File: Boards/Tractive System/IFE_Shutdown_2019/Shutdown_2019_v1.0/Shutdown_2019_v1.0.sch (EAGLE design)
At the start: 195 parts, among them Q1 DMN6140L-7, Q10 DMN6140L-7, Q11 DMP3099L-7, Q12 IRLML6346PBF, Q13 IRLML6346PBF, Q14 IRLML6346PBF, Q15 DMP3099L-7, Q16 DMN6140L-7, Q17 IRLML6346PBF, Q18 DMN6140L-7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

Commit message: nearly done with routing
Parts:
- removed R45: 10k, rcl:R-US_R0603
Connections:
- net +5V: no longer R45.2
- net CANH: now also CAN.2; no longer CAN.1
- net CANL: now also CAN.1; no longer CAN.2
- net HALL_FL_F: now also U2.PA1; no longer U2.PB12
- net HALL_FR_F: now also U2.PA0-WKUP; no longer U2.PB13
- net HALL_RL_F: now also U2.PA2; no longer U2.PB14
- net HALL_RR_F: now also U2.PA3; no longer U2.PB15
- net THROTTLE_OUT: no longer R45.1
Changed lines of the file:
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@@
 <class number="0" name="default" width="0.254" drill="0">
 </class>
-<class number="1" name="PWR" width="0.4064" drill="0">
+<class number="1" name="PWR" width="0.254" drill="0">
 </class>
 <class number="2" name="AIR" width="1.27" drill="0">
 </class>
-<class number="3" name="PWR_IN" width="0.9144" drill="0">
+<class number="3" name="PWR_IN" width="0.4064" drill="0">
 </class>
 </classes>
@@
 <part name="R68" library="rcl" library_urn="urn:adsk.eagle:library:334" deviceset="R-US_" device="R0603" package3d_urn="urn:adsk.eagle:package:23555/2" value="1k"/>
 <part name="P+34" library="supply1" library_urn="urn:adsk.eagle:library:371" deviceset="+5V" device=""/>
-<part name="R45" library="rcl" library_urn="urn:adsk.eagle:library:334" deviceset="R-US_" device="R0603" package3d_urn="urn:adsk.eagle:package:23555/2" value="10k"/>
-<part name="P+35" library="supply1" library_urn="urn:adsk.eagle:library:371" deviceset="+5V" device=""/>
 <part name="R46" library="rcl" library_urn="urn:adsk.eagle:library:334" deviceset="R-US_" device="R0603" package3d_urn="urn:adsk.eagle:package:23555/2" value="10k"/>
 <part name="R69" library="rcl" library_urn="urn:adsk.eagle:library:334" deviceset="R-US_" device="R0603" package3d_urn="urn:adsk.eagle:package:23555/2" value="10k"/>
@@
 </busses>
 <nets>
-<net name="CANH" class="0">
+<net name="CANL" class="0">
 <segment>
 <pinref part="CAN" gate="G$1" pin="1"/>
@@
 </segment>
 </net>
-<net name="CANL" class="0">
-<segment>
-<pinref part="CAN" gate="G$1" pin="2"/>
-<wire x1="-129.54" y1="78.74" x2="-124.46" y2="78.74" width="0.1524" layer="91"/>
-<label x="-124.46" y="78.74" size="1.27" layer="95" xref="yes"/>
-</segment>
-</net>
 <net name="PWR" class="3">
 <segment>
@@
 </segment>
 </net>
+<net name="CANH" class="0">
+<segment>
+<pinref part="CAN" gate="G$1" pin="2"/>
+<wire x1="-129.54" y1="78.74" x2="-124.46" y2="78.74" width="0.1524" layer="91"/>
+<label x="-124.46" y="78.74" size="1.27" layer="95" xref="yes"/>
+</segment>
+</net>
 </nets>
 </sheet>
@@
 <instance part="R68" gate="G$1" x="248.92" y="60.96" rot="R90"/>
 <instance part="P+34" gate="1" x="248.92" y="71.12"/>
-<instance part="R45" gate="G$1" x="332.74" y="193.04" rot="R90"/>
-<instance part="P+35" gate="1" x="332.74" y="203.2"/>
 </instances>
 <busses>
@@
 <net name="HALL_FR_F" class="0">
 <segment>
-<pinref part="U2" gate="A" pin="PB13"/>
-<wire x1="139.7" y1="134.62" x2="137.16" y2="134.62" width="0.1524" layer="91"/>
-<label x="137.16" y="134.62" size="1.27" layer="95" rot="R180" xref="yes"/>
-</segment>
-<segment>
 <pinref part="R60" gate="G$1" pin="2"/>
 <wire x1="264.16" y1="127" x2="266.7" y2="127" width="0.1524" layer="91"/>
@@
 <label x="269.24" y="127" size="1.27" layer="95" xref="yes"/>
 </segment>
-</net>
-<net name="HALL_FL_F" class="0">
 <segment>
-<pinref part="U2" gate="A" pin="PB12"/>
-<wire x1="139.7" y1="137.16" x2="137.16" y2="137.16" width="0.1524" layer="91"/>
-<label x="137.16" y="137.16" size="1.27" layer="95" rot="R180" xref="yes"/>
+<pinref part="U2" gate="A" pin="PA0-WKUP"/>
+<wire x1="139.7" y1="124.46" x2="137.16" y2="124.46" width="0.1524" layer="91"/>
+<label x="137.16" y="124.46" size="1.27" layer="95" rot="R180" xref="yes"/>
 </segment>
+</net>
+<net name="HALL_FL_F" class="0">
 <segment>
 <pinref part="R58" gate="G$1" pin="2"/>
@@
 <label x="269.24" y="162.56" size="1.27" layer="95" xref="yes"/>
 </segment>
-</net>
-<net name="HALL_RL_F" class="0">
 <segment>
-<pinref part="U2" gate="A" pin="PB14"/>
-<wire x1="139.7" y1="132.08" x2="137.16" y2="132.08" width="0.1524" layer="91"/>
-<label x="137.16" y="132.08" size="1.27" layer="95" rot="R180" xref="yes"/>
+<pinref part="U2" gate="A" pin="PA1"/>
+<wire x1="139.7" y1="121.92" x2="137.16" y2="121.92" width="0.1524" layer="91"/>
+<label x="137.16" y="121.92" size="1.27" layer="95" rot="R180" xref="yes"/>
 </segment>
+</net>
+<net name="HALL_RL_F" class="0">
 <segment>
 <pinref part="R62" gate="G$1" pin="2"/>
@@
 <label x="269.24" y="91.44" size="1.27" layer="95" xref="yes"/>
 </segment>
-</net>
-<net name="HALL_RR_F" class="0">
 <segment>
-<pinref part="U2" gate="A" pin="PB15"/>
-<wire x1="139.7" y1="129.54" x2="137.16" y2="129.54" width="0.1524" layer="91"/>
-<label x="137.16" y="129.54" size="1.27" layer="95" rot="R180" xref="yes"/>
+<pinref part="U2" gate="A" pin="PA2"/>
+<wire x1="139.7" y1="119.38" x2="137.16" y2="119.38" width="0.1524" layer="91"/>
+<label x="137.16" y="119.38" size="1.27" layer="95" rot="R180" xref="yes"/>
 </segment>
+</net>
+<net name="HALL_RR_F" class="0">
 <segment>
 <pinref part="R64" gate="G$1" pin="2"/>
@@
 <label x="269.24" y="55.88" size="1.27" layer="95" xref="yes"/>
 </segment>
+<segment>
+<pinref part="U2" gate="A" pin="PA3"/>
+<wire x1="139.7" y1="116.84" x2="137.16" y2="116.84" width="0.1524" layer="91"/>
+<label x="137.16" y="116.84" size="1.27" layer="95" rot="R180" xref="yes"/>
+</segment>
 </net>
 <net name="N$12" class="0">
@@
 <junction x="332.74" y="187.96"/>
 <label x="335.28" y="187.96" size="1.27" layer="95" xref="yes"/>
-<pinref part="R45" gate="G$1" pin="1"/>
 </segment>
 </net>
@@
 <wire x1="248.92" y1="68.58" x2="248.92" y2="66.04" width="0.1524" layer="91"/>
 </segment>
-<segment>
-<pinref part="R45" gate="G$1" pin="2"/>
-<pinref part="P+35" gate="1" pin="+5V"/>
-<wire x1="332.74" y1="198.12" x2="332.74" y2="200.66" width="0.1524" layer="91"/>
-</segment>
 </net>

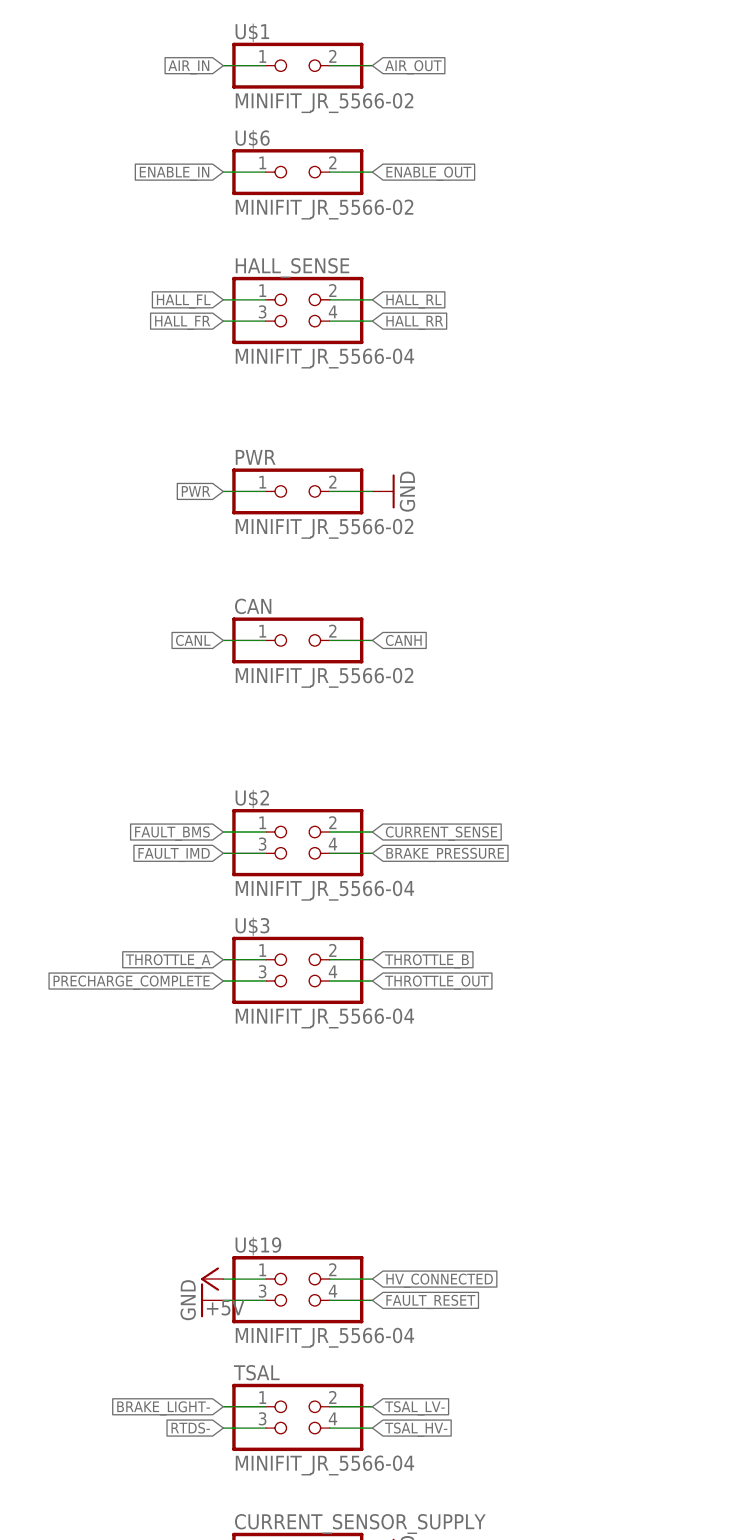
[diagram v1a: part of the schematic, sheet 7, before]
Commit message: Added rounded edges + Silk
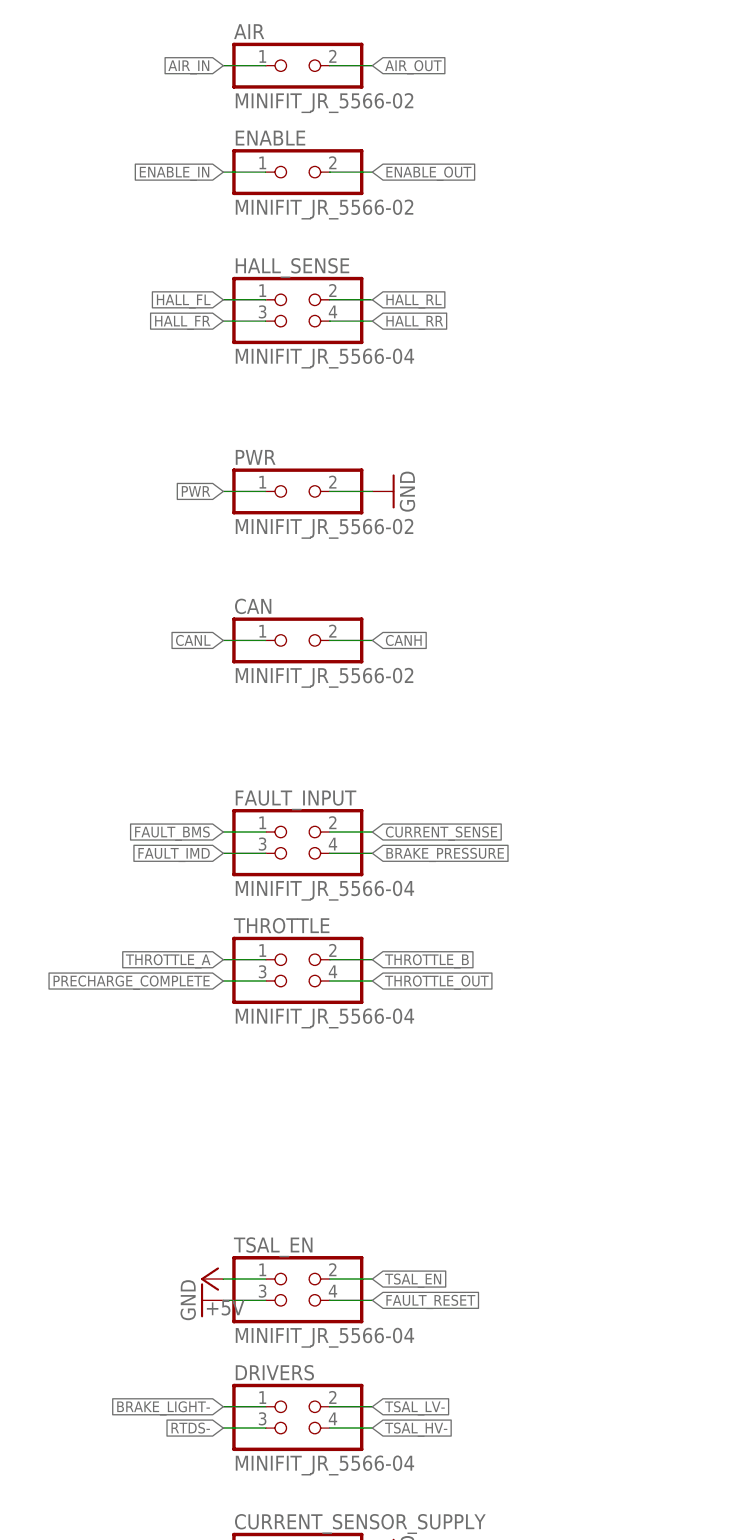
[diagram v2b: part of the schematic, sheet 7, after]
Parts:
- renumbered TSAL to DRIVERS, U$1 to AIR, U$19 to TSAL_EN, U$2 to FAULT_INPUT, U$3 to THROTTLE, U$6 to ENABLE
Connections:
- net HV_CONNECTED renamed TSAL_EN
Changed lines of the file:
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@@
 </classes>
 <parts>
-<part name="TSAL" library="Display_Custom" deviceset="MINIFIT_JR_5566-04" device=""/>
+<part name="DRIVERS" library="Display_Custom" deviceset="MINIFIT_JR_5566-04" device=""/>
 <part name="PWR" library="Display_Custom" deviceset="MINIFIT_JR_5566-02" device=""/>
 <part name="CAN" library="Display_Custom" deviceset="MINIFIT_JR_5566-02" device=""/>
 <part name="GND1" library="supply1" library_urn="urn:adsk.eagle:library:371" deviceset="GND" device=""/>
 <part name="P+2" library="supply1" library_urn="urn:adsk.eagle:library:371" deviceset="+5V" device=""/>
-<part name="U$2" library="Display_Custom" deviceset="MINIFIT_JR_5566-04" device=""/>
-<part name="U$3" library="Display_Custom" deviceset="MINIFIT_JR_5566-04" device=""/>
-<part name="U$1" library="Display_Custom" deviceset="MINIFIT_JR_5566-02" device=""/>
-<part name="U$6" library="Display_Custom" deviceset="MINIFIT_JR_5566-02" device=""/>
+<part name="FAULT_INPUT" library="Display_Custom" deviceset="MINIFIT_JR_5566-04" device=""/>
+<part name="THROTTLE" library="Display_Custom" deviceset="MINIFIT_JR_5566-04" device=""/>
+<part name="AIR" library="Display_Custom" deviceset="MINIFIT_JR_5566-02" device=""/>
+<part name="ENABLE" library="Display_Custom" deviceset="MINIFIT_JR_5566-02" device=""/>
 <part name="HALL_SENSE" library="Display_Custom" deviceset="MINIFIT_JR_5566-04" device=""/>
 <part name="Q5" library="TRANS" deviceset="DMN6140L-7" device=""/>
@@
 <part name="GND67" library="supply1" deviceset="GND" device=""/>
 <part name="GND68" library="supply1" deviceset="GND" device=""/>
-<part name="U$19" library="Display_Custom" deviceset="MINIFIT_JR_5566-04" device=""/>
+<part name="TSAL_EN" library="Display_Custom" deviceset="MINIFIT_JR_5566-04" device=""/>
 <part name="GND63" library="supply1" library_urn="urn:adsk.eagle:library:371" deviceset="GND" device=""/>
 <part name="U$25" library="DIODES_INC" deviceset="BZT52C" device="" value="BZT52C13"/>
@@
 </segment>
 </net>
-<net name="HV_CONNECTED" class="0">
+<net name="TSAL_EN" class="0">
 <segment>
 <pinref part="Q10" gate="G$1" pin="G"/>
@@
 </plain>
 <instances>
-<instance part="TSAL" gate="G$1" x="-132.08" y="-15.24"/>
+<instance part="DRIVERS" gate="G$1" x="-132.08" y="-15.24"/>
 <instance part="PWR" gate="G$1" x="-132.08" y="93.98"/>
 <instance part="CAN" gate="G$1" x="-132.08" y="76.2"/>
 <instance part="GND1" gate="1" x="-121.92" y="96.52" rot="R90"/>
 <instance part="P+2" gate="1" x="-144.78" y="-30.48" rot="R90"/>
-<instance part="U$2" gate="G$1" x="-132.08" y="53.34"/>
-<instance part="U$3" gate="G$1" x="-132.08" y="38.1"/>
-<instance part="U$1" gate="G$1" x="-132.08" y="144.78"/>
-<instance part="U$6" gate="G$1" x="-132.08" y="132.08"/>
+<instance part="FAULT_INPUT" gate="G$1" x="-132.08" y="53.34"/>
+<instance part="THROTTLE" gate="G$1" x="-132.08" y="38.1"/>
+<instance part="AIR" gate="G$1" x="-132.08" y="144.78"/>
+<instance part="ENABLE" gate="G$1" x="-132.08" y="132.08"/>
 <instance part="HALL_SENSE" gate="G$1" x="-132.08" y="116.84"/>
 <instance part="H1" gate="G$1" x="-149.86" y="-66.04"/>
@@
 <instance part="GND67" gate="1" x="53.34" y="63.5"/>
 <instance part="GND68" gate="1" x="53.34" y="30.48"/>
-<instance part="U$19" gate="G$1" x="-132.08" y="0"/>
+<instance part="TSAL_EN" gate="G$1" x="-132.08" y="0"/>
 <instance part="GND63" gate="1" x="-144.78" y="0" rot="R270"/>
 <instance part="U$25" gate="G$1" x="165.1" y="111.76" rot="R90"/>
@@
 </segment>
 <segment>
-<pinref part="U$19" gate="G$1" pin="3"/>
+<pinref part="TSAL_EN" gate="G$1" pin="3"/>
 <wire x1="-137.16" y1="0" x2="-142.24" y2="0" width="0.1524" layer="91"/>
 <pinref part="GND63" gate="1" pin="GND"/>
@@
 <segment>
 <label x="-142.24" y="-12.7" size="1.27" layer="95" rot="R180" xref="yes"/>
-<pinref part="TSAL" gate="G$1" pin="1"/>
+<pinref part="DRIVERS" gate="G$1" pin="1"/>
 <wire x1="-137.16" y1="-12.7" x2="-142.24" y2="-12.7" width="0.1524" layer="91"/>
 </segment>
@@
 <net name="TSAL_LV-" class="0">
 <segment>
-<pinref part="TSAL" gate="G$1" pin="2"/>
+<pinref part="DRIVERS" gate="G$1" pin="2"/>
 <wire x1="-129.54" y1="-12.7" x2="-124.46" y2="-12.7" width="0.1524" layer="91"/>
 <label x="-124.46" y="-12.7" size="1.27" layer="95" xref="yes"/>
@@
 <net name="TSAL_HV-" class="0">
 <segment>
-<pinref part="TSAL" gate="G$1" pin="4"/>
+<pinref part="DRIVERS" gate="G$1" pin="4"/>
 <wire x1="-129.54" y1="-15.24" x2="-124.46" y2="-15.24" width="0.1524" layer="91"/>
 <label x="-124.46" y="-15.24" size="1.27" layer="95" xref="yes"/>
@@
 <net name="CURRENT_SENSE" class="0">
 <segment>
-<pinref part="U$2" gate="G$1" pin="2"/>
+<pinref part="FAULT_INPUT" gate="G$1" pin="2"/>
 <wire x1="-129.54" y1="55.88" x2="-124.46" y2="55.88" width="0.1524" layer="91"/>
 <label x="-124.46" y="55.88" size="1.27" layer="95" xref="yes"/>
@@
 <net name="BRAKE_PRESSURE" class="0">
 <segment>
-<pinref part="U$2" gate="G$1" pin="4"/>
+<pinref part="FAULT_INPUT" gate="G$1" pin="4"/>
 <wire x1="-129.54" y1="53.34" x2="-124.46" y2="53.34" width="0.1524" layer="91"/>
 <label x="-124.46" y="53.34" size="1.27" layer="95" xref="yes"/>
@@
 <net name="THROTTLE_A" class="0">
 <segment>
-<pinref part="U$3" gate="G$1" pin="1"/>
+<pinref part="THROTTLE" gate="G$1" pin="1"/>
 <wire x1="-137.16" y1="40.64" x2="-142.24" y2="40.64" width="0.1524" layer="91"/>
 <label x="-142.24" y="40.64" size="1.27" layer="95" rot="R180" xref="yes"/>
@@
 <net name="THROTTLE_B" class="0">
 <segment>
-<pinref part="U$3" gate="G$1" pin="2"/>
+<pinref part="THROTTLE" gate="G$1" pin="2"/>
 <wire x1="-129.54" y1="40.64" x2="-124.46" y2="40.64" width="0.1524" layer="91"/>
 <label x="-124.46" y="40.64" size="1.27" layer="95" xref="yes"/>
@@
 <net name="THROTTLE_OUT" class="0">
 <segment>
-<pinref part="U$3" gate="G$1" pin="4"/>
+<pinref part="THROTTLE" gate="G$1" pin="4"/>
 <wire x1="-129.54" y1="38.1" x2="-124.46" y2="38.1" width="0.1524" layer="91"/>
 <label x="-124.46" y="38.1" size="1.27" layer="95" xref="yes"/>
 </segment>
 </net>
-<net name="HV_CONNECTED" class="0">
+<net name="TSAL_EN" class="0">
 <segment>
 <wire x1="-129.54" y1="2.54" x2="-124.46" y2="2.54" width="0.1524" layer="91"/>
 <label x="-124.46" y="2.54" size="1.27" layer="95" xref="yes"/>
-<pinref part="U$19" gate="G$1" pin="2"/>
+<pinref part="TSAL_EN" gate="G$1" pin="2"/>
 </segment>
 </net>
@@
 <segment>
 <label x="-124.46" y="0" size="1.27" layer="95" xref="yes"/>
-<pinref part="U$19" gate="G$1" pin="4"/>
+<pinref part="TSAL_EN" gate="G$1" pin="4"/>
 <wire x1="-124.46" y1="0" x2="-129.54" y2="0" width="0.1524" layer="91"/>
 </segment>
@@
 <net name="AIR_IN" class="0">
 <segment>
-<pinref part="U$1" gate="G$1" pin="1"/>
+<pinref part="AIR" gate="G$1" pin="1"/>
 <wire x1="-137.16" y1="147.32" x2="-142.24" y2="147.32" width="0.1524" layer="91"/>
 <label x="-142.24" y="147.32" size="1.27" layer="95" rot="R180" xref="yes"/>
@@
 <net name="AIR_OUT" class="0">
 <segment>
-<pinref part="U$1" gate="G$1" pin="2"/>
+<pinref part="AIR" gate="G$1" pin="2"/>
 <wire x1="-129.54" y1="147.32" x2="-124.46" y2="147.32" width="0.1524" layer="91"/>
 <label x="-124.46" y="147.32" size="1.27" layer="95" xref="yes"/>
@@
 <net name="ENABLE_IN" class="0">
 <segment>
-<pinref part="U$6" gate="G$1" pin="1"/>
+<pinref part="ENABLE" gate="G$1" pin="1"/>
 <wire x1="-137.16" y1="134.62" x2="-142.24" y2="134.62" width="0.1524" layer="91"/>
 <label x="-142.24" y="134.62" size="1.27" layer="95" rot="R180" xref="yes"/>
@@
 <net name="ENABLE_OUT" class="0">
 <segment>
-<pinref part="U$6" gate="G$1" pin="2"/>
+<pinref part="ENABLE" gate="G$1" pin="2"/>
 <wire x1="-129.54" y1="134.62" x2="-124.46" y2="134.62" width="0.1524" layer="91"/>
 <label x="-124.46" y="134.62" size="1.27" layer="95" xref="yes"/>
@@
 <net name="PRECHARGE_COMPLETE" class="0">
 <segment>
-<pinref part="U$3" gate="G$1" pin="3"/>
+<pinref part="THROTTLE" gate="G$1" pin="3"/>
 <wire x1="-137.16" y1="38.1" x2="-142.24" y2="38.1" width="0.1524" layer="91"/>
 <label x="-142.24" y="38.1" size="1.27" layer="95" rot="R180" xref="yes"/>
@@
 <net name="RTDS-" class="0">
 <segment>
-<pinref part="TSAL" gate="G$1" pin="3"/>
+<pinref part="DRIVERS" gate="G$1" pin="3"/>
 <wire x1="-137.16" y1="-15.24" x2="-142.24" y2="-15.24" width="0.1524" layer="91"/>
 <label x="-142.24" y="-15.24" size="1.27" layer="95" rot="R180" xref="yes"/>
@@
 <wire x1="-137.16" y1="2.54" x2="-142.24" y2="2.54" width="0.1524" layer="91"/>
 <pinref part="P+18" gate="1" pin="+5V"/>
-<pinref part="U$19" gate="G$1" pin="1"/>
+<pinref part="TSAL_EN" gate="G$1" pin="1"/>
 </segment>
 <segment>
@@
 </segment>
 <segment>
-<pinref part="U$2" gate="G$1" pin="1"/>
+<pinref part="FAULT_INPUT" gate="G$1" pin="1"/>
 <wire x1="-137.16" y1="55.88" x2="-142.24" y2="55.88" width="0.1524" layer="91"/>
 <label x="-142.24" y="55.88" size="1.27" layer="95" rot="R180" xref="yes"/>
@@
 </segment>
 <segment>
-<pinref part="U$2" gate="G$1" pin="3"/>
+<pinref part="FAULT_INPUT" gate="G$1" pin="3"/>
 <wire x1="-137.16" y1="53.34" x2="-142.24" y2="53.34" width="0.1524" layer="91"/>
 <label x="-142.24" y="53.34" size="1.27" layer="95" rot="R180" xref="yes"/>
